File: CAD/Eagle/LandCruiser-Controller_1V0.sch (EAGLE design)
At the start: 60 parts, among them K311 V23086C1001A403, K312 V23086C1001A403, K313 V23086C1001A403, K314 V23086C1001A403, K315 V23086C1001A403, U101 MEGA8-P, U221 SN75240, U301 MIC2981/2982SO18W, U501 MAX232_SOIC16, U611 LM7805, X201 WEIDMUELLER 1234600000, X321 WEIDMUELLER 1234600000, X401 I2C

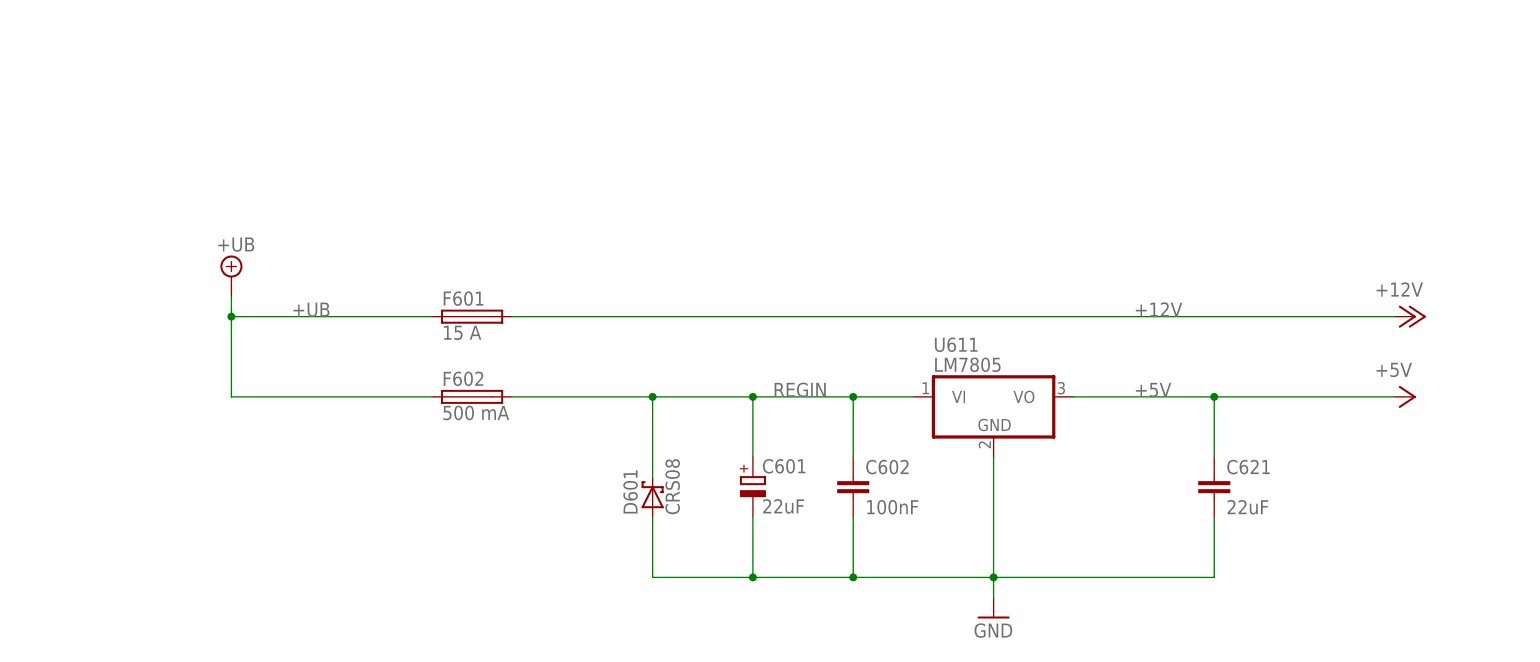
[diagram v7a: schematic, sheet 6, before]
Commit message: HW_V1.0 - status LED added, ADC0 connected to 15:1 divider for 12V control
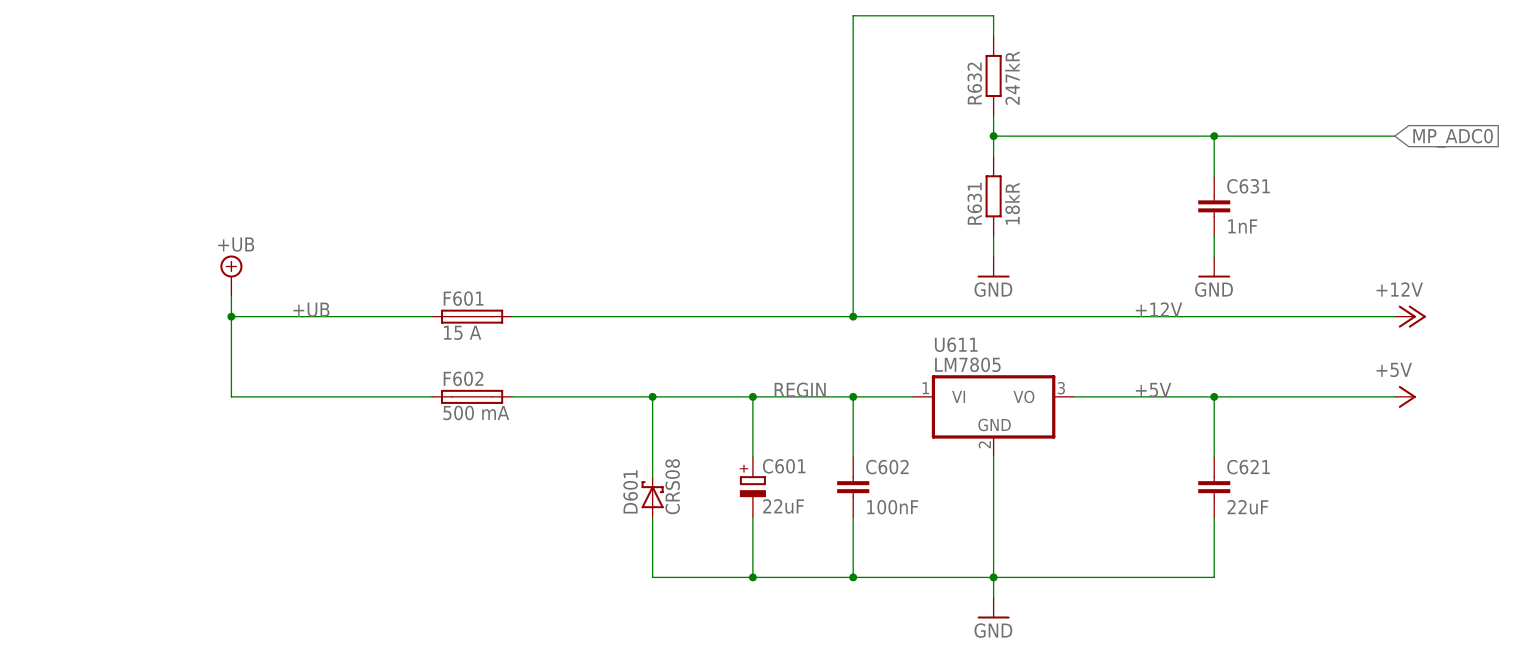
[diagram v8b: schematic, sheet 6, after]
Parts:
- added C631: 1nF, rcl:C-EUC0805
- added D141: red, df4iah_diode:LED
- added R141: 330R, rcl:R-EU_R0805
- added R631: 18kR, rcl:R-EU_R0805
- added R632: 247kR, rcl:R-EU_R0805
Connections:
- new net LED_A: D141.A, R141.2
- new net MP_ADC0: C631.1, R631.2, R632.1, U101.PC0(ADC0)
- new net MP_ADC1: U101.PC1(ADC1)
- new net MP_LED: R141.1, U101.PD3(INT1)
- net +12V: now also R632.2
- net GND: now also C631.2, D141.C, R631.1
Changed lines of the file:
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@@
 <part name="U221" library="df4iah_esd" deviceset="SN75240" device=""/>
 <part name="GND221" library="df4iah_supply" deviceset="GND" device=""/>
-<part name="GND1" library="df4iah_supply" deviceset="GND" device=""/>
+<part name="GND222" library="df4iah_supply" deviceset="GND" device=""/>
 <part name="U301" library="df4iah_dataconvertion" deviceset="MIC2981/2982" device="SO18W"/>
 <part name="GND302" library="df4iah_supply" deviceset="GND" device=""/>
@@
 <part name="R211" library="rcl" deviceset="R-EU_" device="R0805" value="22kR"/>
 <part name="R231" library="rcl" deviceset="R-EU_" device="R0805" value="10kR"/>
-<part name="GND2" library="df4iah_supply" deviceset="GND" device=""/>
+<part name="GND231" library="df4iah_supply" deviceset="GND" device=""/>
 <part name="F601" library="df4iah_fuse" deviceset="MCCQ-121" device="" value="15 A"/>
 <part name="F602" library="df4iah_fuse" deviceset="MCCQ-121" device="" value="500 mA"/>
@@
 <part name="C602" library="rcl" deviceset="C-EU" device="C0805" value="100nF"/>
 <part name="C301" library="rcl" deviceset="C-EU" device="C0805" value="100nF"/>
+<part name="R141" library="rcl" deviceset="R-EU_" device="R0805" value="330R"/>
+<part name="D141" library="df4iah_diode" deviceset="LED" device="" value="red"/>
+<part name="GND141" library="df4iah_supply" deviceset="GND" device=""/>
+<part name="GND631" library="df4iah_supply" deviceset="GND" device=""/>
+<part name="R631" library="rcl" deviceset="R-EU_" device="R0805" value="18kR"/>
+<part name="R632" library="rcl" deviceset="R-EU_" device="R0805" value="247kR"/>
+<part name="C631" library="rcl" deviceset="C-EU" device="C0805" value="1nF"/>
+<part name="GND632" library="df4iah_supply" deviceset="GND" device=""/>
 </parts>
 <sheets>
@@
 <instance part="R123" gate="G$1" x="58.42" y="81.28" rot="R90"/>
 <instance part="R124" gate="G$1" x="68.58" y="81.28" rot="R90"/>
+<instance part="R141" gate="G$1" x="180.34" y="88.9"/>
+<instance part="D141" gate="G$1" x="198.12" y="83.82"/>
+<instance part="GND141" gate="1" x="198.12" y="76.2"/>
 </instances>
 <busses>
@@
 <pinref part="GND111" gate="1" pin="GND"/>
 <wire x1="134.62" y1="139.7" x2="134.62" y2="149.86" width="0.1524" layer="91"/>
+</segment>
+<segment>
+<pinref part="D141" gate="G$1" pin="C"/>
+<pinref part="GND141" gate="1" pin="GND"/>
 </segment>
 </net>
@@
 </segment>
 </net>
+<net name="MP_LED" class="0">
+<segment>
+<pinref part="U101" gate="G$1" pin="PD3(INT1)"/>
+<wire x1="160.02" y1="88.9" x2="175.26" y2="88.9" width="0.1524" layer="91"/>
+<pinref part="R141" gate="G$1" pin="1"/>
+</segment>
+</net>
+<net name="LED_A" class="0">
+<segment>
+<pinref part="R141" gate="G$1" pin="2"/>
+<wire x1="185.42" y1="88.9" x2="198.12" y2="88.9" width="0.1524" layer="91"/>
+<pinref part="D141" gate="G$1" pin="A"/>
+<wire x1="198.12" y1="88.9" x2="198.12" y2="86.36" width="0.1524" layer="91"/>
+</segment>
+</net>
+<net name="MP_ADC0" class="0">
+<segment>
+<pinref part="U101" gate="G$1" pin="PC0(ADC0)"/>
+<wire x1="160.02" y1="119.38" x2="226.06" y2="119.38" width="0.1524" layer="91"/>
+<label x="226.06" y="119.38" size="1.778" layer="95" xref="yes"/>
+</segment>
+</net>
+<net name="MP_ADC1" class="0">
+<segment>
+<pinref part="U101" gate="G$1" pin="PC1(ADC1)"/>
+<wire x1="160.02" y1="116.84" x2="226.06" y2="116.84" width="0.1524" layer="91"/>
+<label x="226.06" y="116.84" size="1.778" layer="95" xref="yes"/>
+</segment>
+</net>
 </nets>
 </sheet>
@@
 <instance part="U221" gate="G$1" x="129.54" y="63.5"/>
 <instance part="GND221" gate="1" x="101.6" y="53.34"/>
-<instance part="GND1" gate="1" x="157.48" y="53.34"/>
+<instance part="GND222" gate="1" x="157.48" y="53.34"/>
 <instance part="R211" gate="G$1" x="127" y="162.56" rot="R90"/>
 <instance part="R231" gate="G$1" x="127" y="147.32" rot="R90"/>
-<instance part="GND2" gate="1" x="127" y="137.16"/>
+<instance part="GND231" gate="1" x="127" y="137.16"/>
 </instances>
 <busses>
@@
 <segment>
 <wire x1="157.48" y1="66.04" x2="157.48" y2="55.88" width="0.1524" layer="91"/>
-<pinref part="GND1" gate="1" pin="GND"/>
+<pinref part="GND222" gate="1" pin="GND"/>
 <wire x1="157.48" y1="66.04" x2="144.78" y2="66.04" width="0.1524" layer="91"/>
 <wire x1="157.48" y1="55.88" x2="144.78" y2="55.88" width="0.1524" layer="91"/>
@@
 <segment>
 <pinref part="R231" gate="G$1" pin="1"/>
-<pinref part="GND2" gate="1" pin="GND"/>
+<pinref part="GND231" gate="1" pin="GND"/>
 <wire x1="127" y1="142.24" x2="127" y2="139.7" width="0.1524" layer="91"/>
 </segment>
@@
 <instance part="F602" gate="G$1" x="83.82" y="96.52"/>
 <instance part="C602" gate="G$1" x="132.08" y="86.36"/>
+<instance part="GND631" gate="1" x="149.86" y="111.76"/>
+<instance part="R631" gate="G$1" x="149.86" y="121.92" rot="R90"/>
+<instance part="R632" gate="G$1" x="149.86" y="137.16" rot="R90"/>
+<instance part="C631" gate="G$1" x="177.8" y="121.92"/>
+<instance part="GND632" gate="1" x="177.8" y="111.76"/>
 </instances>
 <busses>
@@
 <junction x="132.08" y="73.66"/>
 </segment>
+<segment>
+<wire x1="149.86" y1="116.84" x2="149.86" y2="114.3" width="0.1524" layer="91"/>
+<pinref part="GND631" gate="1" pin="GND"/>
+<pinref part="R631" gate="G$1" pin="1"/>
+</segment>
+<segment>
+<pinref part="GND632" gate="1" pin="GND"/>
+<pinref part="C631" gate="G$1" pin="2"/>
+<wire x1="177.8" y1="114.3" x2="177.8" y2="116.84" width="0.1524" layer="91"/>
+</segment>
 </net>
 <net name="+5V" class="2">
@@
 <segment>
 <pinref part="P+12V_601" gate="1" pin="+12V"/>
-<wire x1="200.66" y1="106.68" x2="88.9" y2="106.68" width="0.1524" layer="91"/>
+<wire x1="200.66" y1="106.68" x2="132.08" y2="106.68" width="0.1524" layer="91"/>
 <label x="167.64" y="106.68" size="1.778" layer="95"/>
 <pinref part="F601" gate="G$1" pin="2"/>
+<wire x1="132.08" y1="106.68" x2="88.9" y2="106.68" width="0.1524" layer="91"/>
+<wire x1="132.08" y1="106.68" x2="132.08" y2="144.78" width="0.1524" layer="91"/>
+<wire x1="132.08" y1="144.78" x2="149.86" y2="144.78" width="0.1524" layer="91"/>
+<wire x1="149.86" y1="144.78" x2="149.86" y2="142.24" width="0.1524" layer="91"/>
+<junction x="132.08" y="106.68"/>
+<pinref part="R632" gate="G$1" pin="2"/>
 </segment>
 </net>
@@
 </segment>
 </net>
+<net name="MP_ADC0" class="0">
+<segment>
+<wire x1="149.86" y1="132.08" x2="149.86" y2="129.54" width="0.1524" layer="91"/>
+<wire x1="149.86" y1="129.54" x2="149.86" y2="127" width="0.1524" layer="91"/>
+<wire x1="149.86" y1="129.54" x2="177.8" y2="129.54" width="0.1524" layer="91"/>
+<label x="200.66" y="129.54" size="1.778" layer="95" xref="yes"/>
+<pinref part="R631" gate="G$1" pin="2"/>
+<pinref part="R632" gate="G$1" pin="1"/>
+<junction x="149.86" y="129.54"/>
+<pinref part="C631" gate="G$1" pin="1"/>
+<wire x1="177.8" y1="129.54" x2="200.66" y2="129.54" width="0.1524" layer="91"/>
+<wire x1="177.8" y1="124.46" x2="177.8" y2="129.54" width="0.1524" layer="91"/>
+<junction x="177.8" y="129.54"/>
+</segment>
+</net>
